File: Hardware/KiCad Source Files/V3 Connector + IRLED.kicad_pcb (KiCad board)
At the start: 2 copper layers, 60 x 126.6 mm, 151 parts, among them J1 YK3210203000G, J2 USB4085-GF-A, J3 Conn_01x08, J4 YK3210203000G, J5 USB4085-GF-A, J6 USB1125-GF-B, Q1 IRLU024NPBF, Q2 IRLU024NPBF, Q3 Q_NMOS, U1 MC33063AP, U4 LM4040LP-2.0, U5 MCP4801, U6 MCP3202

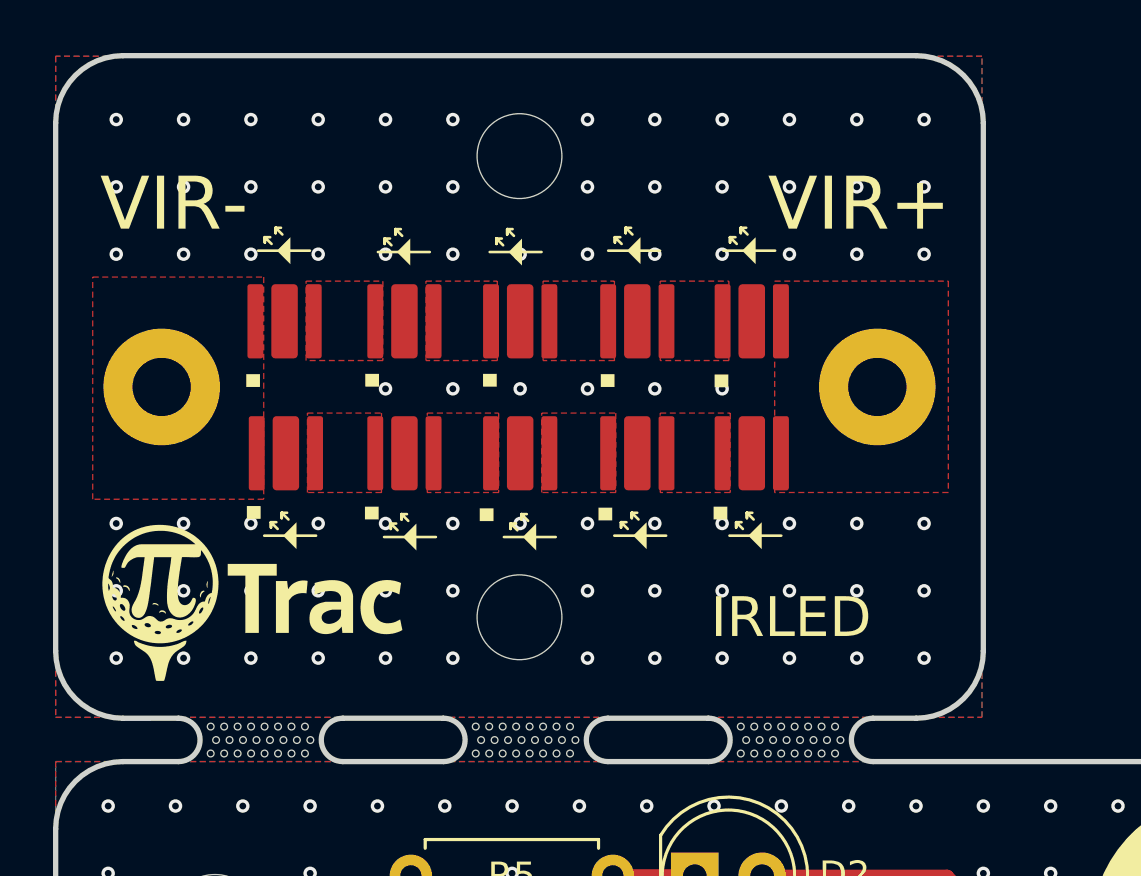
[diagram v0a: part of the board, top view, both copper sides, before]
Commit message: Replace IRLED1 [Original] with IRLED2. Fixes problem supporting cheap IRLED we found right before heading to fabrication.
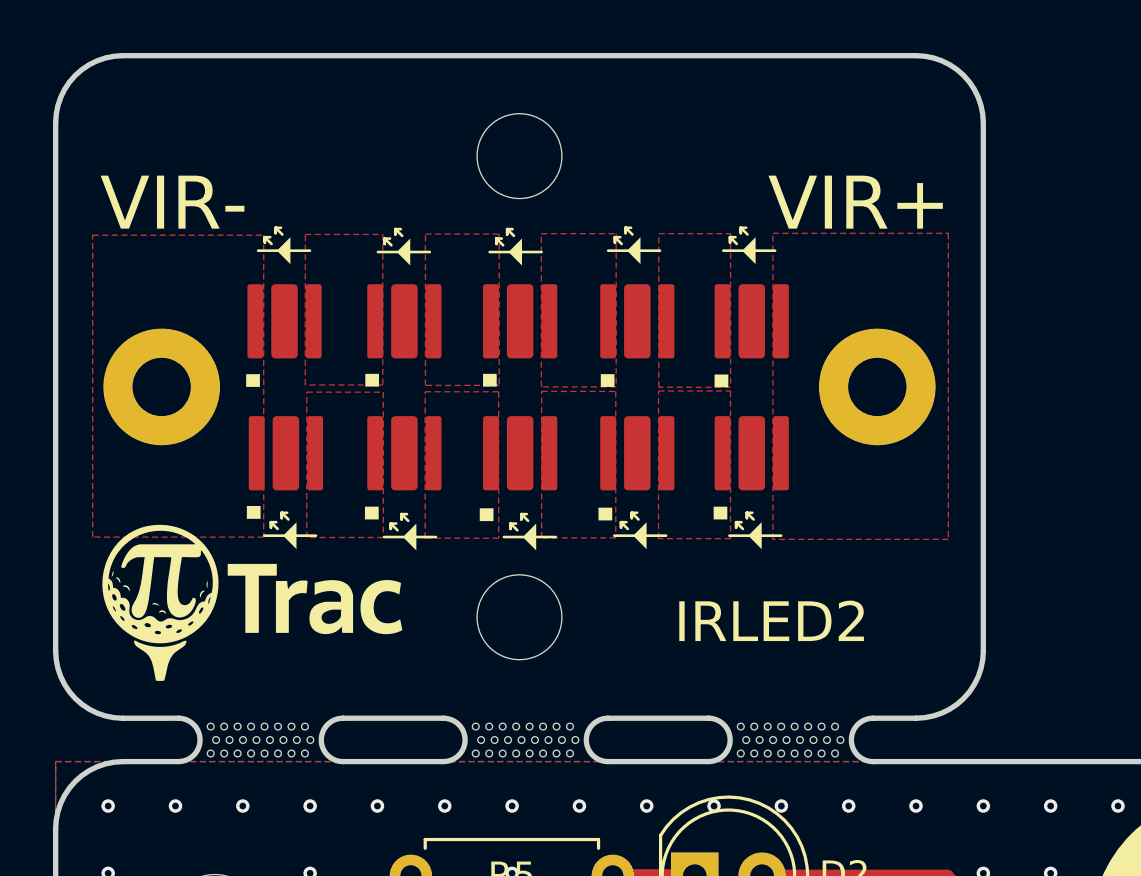
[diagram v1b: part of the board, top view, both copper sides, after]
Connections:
- D10 pad 3: Net-(D10-P) -> unconnected-(D10-P-Pad3)
- D11 pad 3: Net-(D10-P) -> unconnected-(D11-P-Pad3)
- D12 pad 3: Net-(D10-P) -> unconnected-(D12-P-Pad3)
- D13 pad 3: Net-(D10-P) -> unconnected-(D13-P-Pad3)
- D14 pad 3: Net-(D10-P) -> unconnected-(D14-P-Pad3)
- D15 pad 3: Net-(D10-P) -> unconnected-(D15-P-Pad3)
- D6 pad 3: Net-(D10-P) -> unconnected-(D6-P-Pad3)
- D7 pad 3: Net-(D10-P) -> unconnected-(D7-P-Pad3)
- D8 pad 3: Net-(D10-P) -> unconnected-(D8-P-Pad3)
- D9 pad 3: Net-(D10-P) -> unconnected-(D9-P-Pad3)
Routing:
- net Net-(D10-P): vias 80 -> 0
- removed copper zone on B.Cu, net Net-(D10-P)
- removed copper zone on F.Cu, net Net-(D10-P)
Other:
- board text added: "IRLED2"
- board text removed: "IRLED"
